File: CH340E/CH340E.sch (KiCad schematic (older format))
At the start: 19 parts, among them J2 Conn_01x06, P1 USB_C_Plug_USB2.0, U1 CH340E, U2 AP2127K-3.3

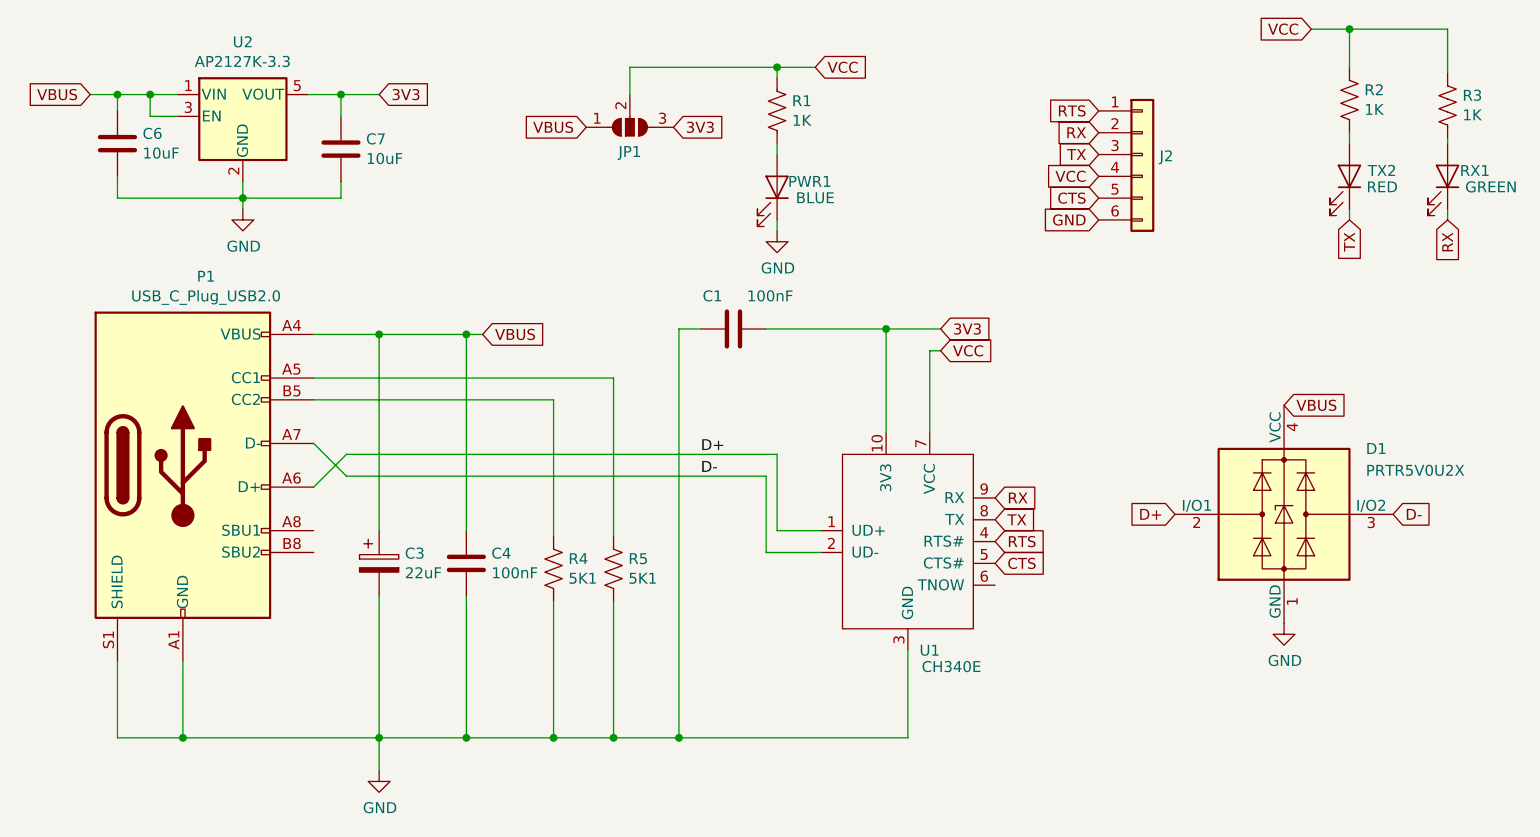
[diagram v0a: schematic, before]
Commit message: SirUSB Board Revisions
Removed MicroUSB Versions of FT230 and FT231, SolderPaste Layer Adjusted to -0.05mm, Silkscreens optimised, OSHW logo added.
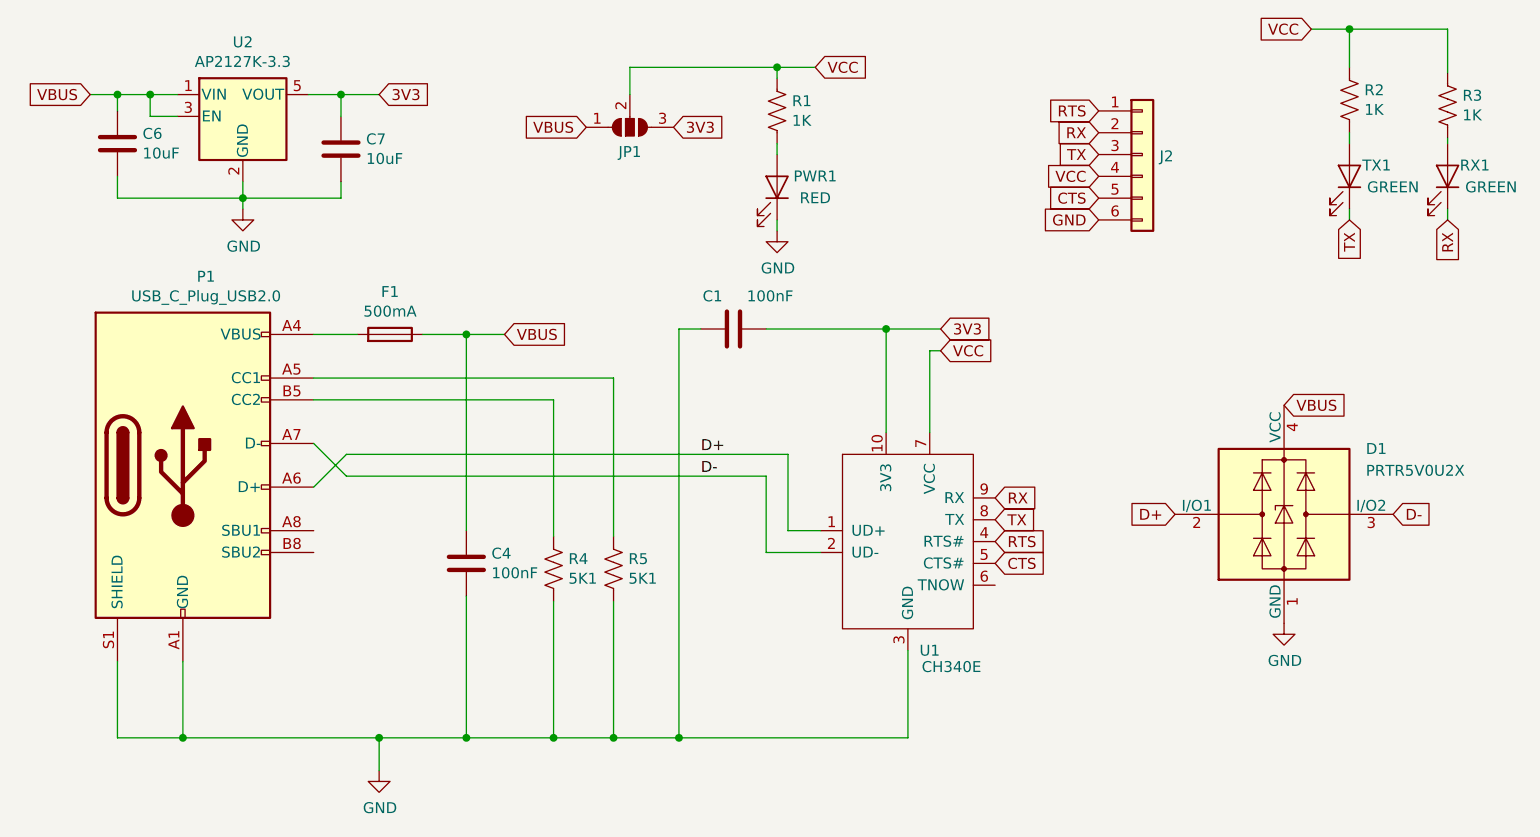
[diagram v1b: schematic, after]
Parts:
- removed C3: 22uF, Capacitor_Tantalum_SMD:CP_EIA-3216-18_Kemet-A_Pad1.58x1.35mm_HandSolder, symbol Device:CP
- added F1: 500mA, Fuse:Fuse_0805_2012Metric, symbol Device:Fuse
- PWR1: value BLUE -> RED; Part C193191 -> C118330
- TX1: renamed from TX2; value RED -> GREEN; Part C118330 -> C205443
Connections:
- net VBUS: now also F1.1; no longer P1.A4 (VBUS), P1.A9 (VBUS), P1.B4 (VBUS), P1.B9 (VBUS)
- new net: F1.2, P1.A4 (VBUS), P1.A9 (VBUS), P1.B4 (VBUS), P1.B9 (VBUS)
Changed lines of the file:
@@
 Sheet 1 1
 Title "CH340E USB to UART converter"
-Date "2020-04-13"
-Rev "1.1"
+Date "2020-04-21"
+Rev "1.2"
 Comp "SirBoard"
 Comment1 "www.SirBoard.com"
@@
 	1    0    0    -1
 $EndComp
-$Comp
-L Device:CP C3
-U 1 1 5D25E8A7
-P 2350 3100
-F 0 "C3" H 2468 3145 50  0000 L CNN
-F 1 "22uF" H 2468 3055 50  0000 L CNN
-F 2 "Capacitor_Tantalum_SMD:CP_EIA-3216-18_Kemet-A_Pad1.58x1.35mm_HandSolder" H 2388 2950 50  0001 C CNN
-F 3 "~" H 2350 3100 50  0001 C CNN
-F 4 "C122643" H 2350 3100 50  0001 C CNN "Part"
-	1    2350 3100
-	1    0    0    -1
-$EndComp
 Wire Wire Line
 	4775 3500 4775 3900
 Wire Wire Line
-	4375 2950 4175 2950
-Wire Wire Line
-	4175 2950 4175 2600
+	4375 2950 4225 2950
+Wire Wire Line
+	4225 2950 4225 2600
 Wire Wire Line
 	4125 2700 4125 3050
@@
 	4125 3050 4375 3050
 Wire Wire Line
-	2350 2950 2350 2050
-Wire Wire Line
 	2750 2950 2750 2050
-Wire Wire Line
-	2350 3250 2350 3900
 Wire Wire Line
 	2750 3250 2750 3900
@@
 	2200 2600 2050 2750
 Wire Wire Line
-	2200 2600 4175 2600
+	2200 2600 4225 2600
 Wire Wire Line
 	2200 2700 2050 2550
@@
 	1450 3900 2350 3900
 Connection ~ 2350 3900
-Text GLabel 2825 2050 2    50   Input ~ 0
+Text GLabel 2925 2050 2    50   Input ~ 0
 VBUS
 Wire Wire Line
-	2825 2050 2750 2050
+	2925 2050 2750 2050
 $Comp
 L power:GND #PWR0101
@@
 U 1 1 5E4CEE4C
 P 7250 1325
-F 0 "RX1" V 7275 1450 50  0000 C CNN
+F 0 "RX1" V 7300 1450 50  0000 C CNN
 F 1 "GREEN" V 7200 1525 50  0000 C CNN
 F 2 "LED_SMD:LED_0603_1608Metric" H 7250 1325 50  0001 C CNN
@@
 $EndComp
 $Comp
-L Device:LED TX2
+L Device:LED TX1
 U 1 1 5E4E74BC
 P 6800 1325
-F 0 "TX2" V 6825 1475 50  0000 C CNN
-F 1 "RED" V 6750 1475 50  0000 C CNN
+F 0 "TX1" V 6850 1450 50  0000 C CNN
+F 1 "GREEN" V 6750 1525 50  0000 C CNN
 F 2 "LED_SMD:LED_0603_1608Metric" H 6800 1325 50  0001 C CNN
 F 3 "~" H 6800 1325 50  0001 C CNN
-F 4 "C118330" H 6800 1325 50  0001 C CNN "Part"
+F 4 "C205443" H 6800 1325 50  0001 C CNN "Part"
 	1    6800 1325
 	0    1    -1   0
@@
 U 1 1 5E4F8641
 P 4175 1375
-F 0 "PWR1" V 4200 1525 50  0000 C CNN
-F 1 "BLUE" V 4125 1550 50  0000 C CNN
+F 0 "PWR1" V 4225 1550 50  0000 C CNN
+F 1 "RED" V 4125 1550 50  0000 C CNN
 F 2 "LED_SMD:LED_0603_1608Metric" H 4175 1375 50  0001 C CNN
 F 3 "~" H 4175 1375 50  0001 C CNN
-F 4 "C193191" H 4175 1375 50  0001 C CNN "Part"
+F 4 "C118330" H 4175 1375 50  0001 C CNN "Part"
 	1    4175 1375
 	0    1    -1   0
@@
 Wire Wire Line
 	3725 3900 4775 3900
-Connection ~ 2750 2050
 Connection ~ 2750 3900
 Wire Wire Line
 	2750 3900 3150 3900
-Wire Wire Line
-	2350 2050 2750 2050
 Wire Wire Line
 	2350 3900 2750 3900
@@
 Wire Wire Line
 	3425 3900 3725 3900
-Wire Wire Line
-	2050 2050 2350 2050
-Connection ~ 2350 2050
+$Comp
+L Device:Fuse F1
+U 1 1 5EAFB1BD
+P 2400 2050
+F 0 "F1" V 2595 2050 50  0000 C CNN
+F 1 "500mA" V 2505 2050 50  0000 C CNN
+F 2 "Fuse:Fuse_0805_2012Metric" V 2330 2050 50  0001 C CNN
+F 3 "~" H 2400 2050 50  0001 C CNN
+F 4 "C89657" V 2400 2050 50  0001 C CNN "Part"
+	1    2400 2050
+	0    1    -1   0
+$EndComp
+Wire Wire Line
+	2250 2050 2050 2050
+Wire Wire Line
+	2550 2050 2750 2050
+Connection ~ 2750 2050
 $EndSCHEMATC
